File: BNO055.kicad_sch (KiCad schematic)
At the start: 7 parts, among them Y1 32.768kHz

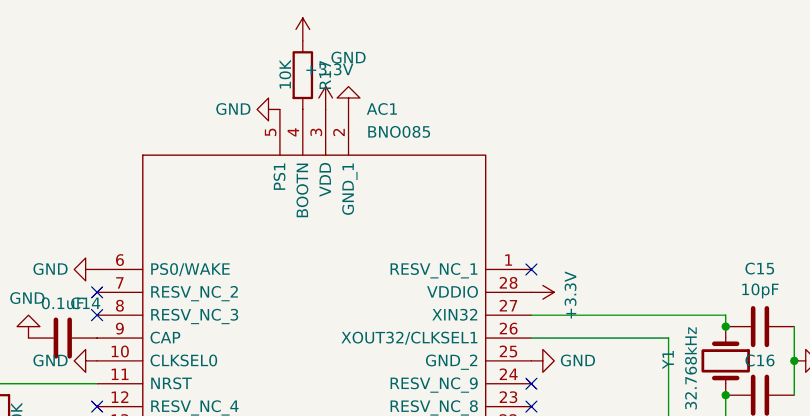
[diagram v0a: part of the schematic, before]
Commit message: Addressing the issues with the sample version, Updating the bom to source all the correct components from the JLCPCB supply
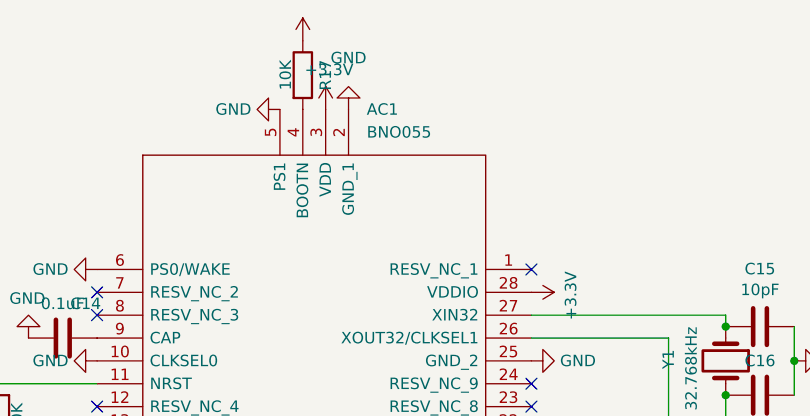
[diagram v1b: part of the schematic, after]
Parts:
- AC1: value BNO085 -> BNO055
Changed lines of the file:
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@@
       (effects (font (size 1.27 1.27)) (justify left))
     )
-    (property "Value" "BNO085" (id 1) (at 168.3894 66.04 0)
+    (property "Value" "BNO055" (id 1) (at 168.3894 66.04 0)
       (effects (font (size 1.27 1.27)) (justify left))
     )
